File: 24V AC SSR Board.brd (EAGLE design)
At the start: 96.5 x 63.5 mm, 45 parts, among them X1 1751293

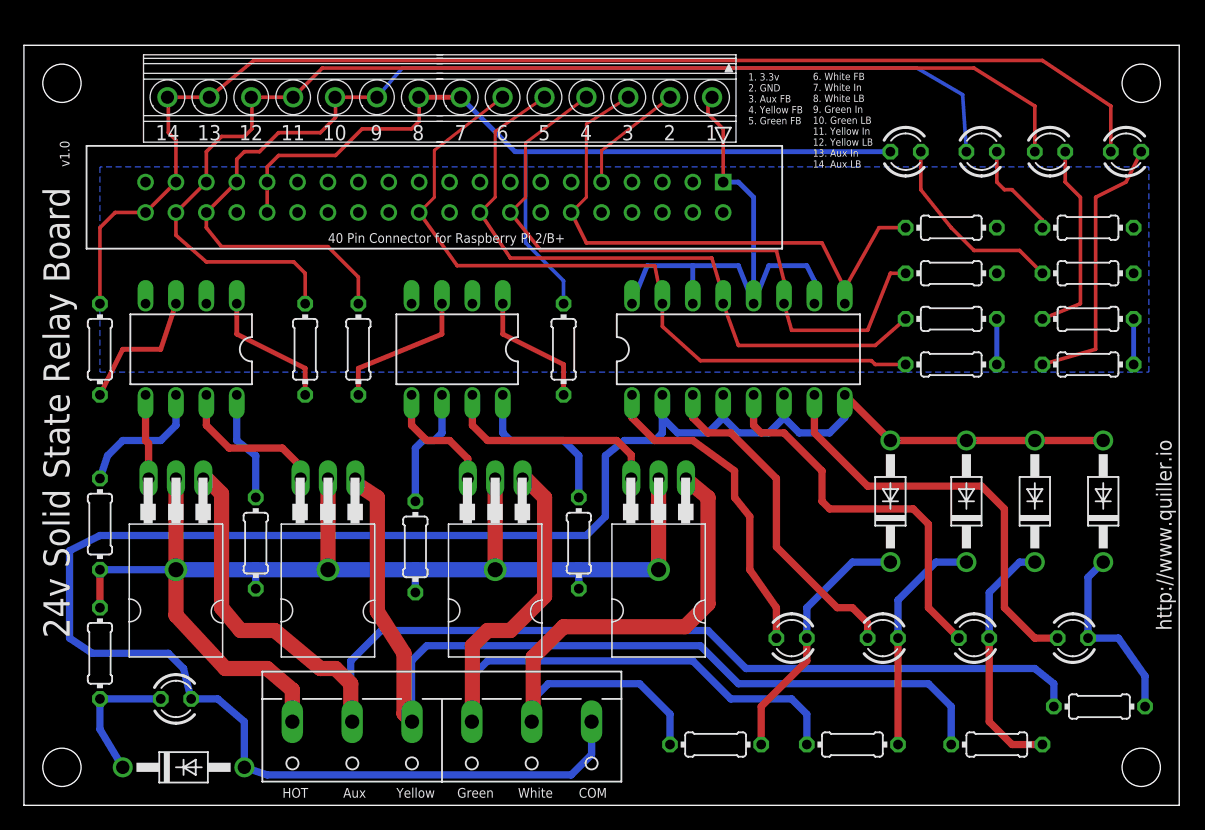
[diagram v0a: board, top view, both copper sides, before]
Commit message: Added Photon Board schematics and board
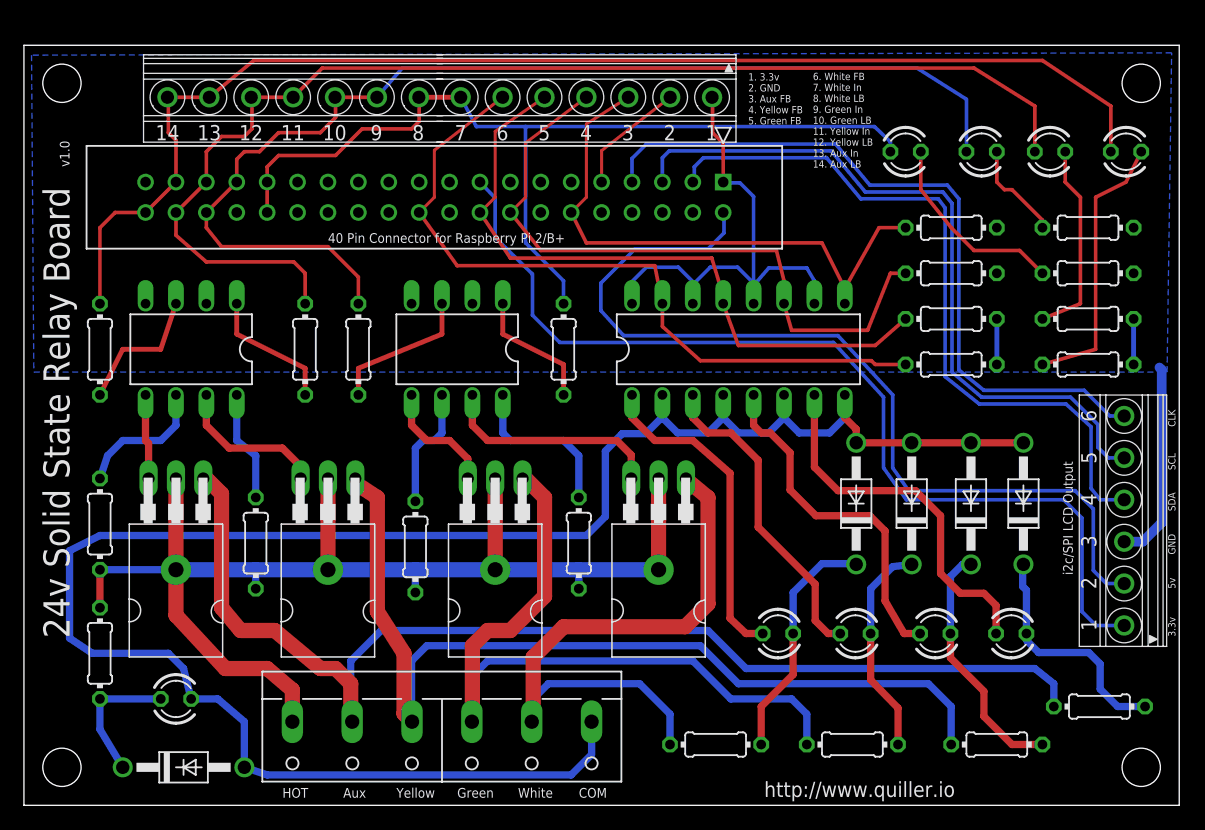
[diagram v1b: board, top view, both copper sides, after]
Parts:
- added T3-: (no value), myhvac:6-POS-SCREW-TERM-PT-3.5MM
- R18, R19, R20, R21: value 4.7K -> 100K
- TERM: value (none) -> OUT BLOCK
- moved D5 6.67 mm to (83.5, 25.2)
- moved D4 5.34 mm to (79.1, 25.2)
- moved LED_OUT_A 5.16 mm to (82.5, 14.4)
- moved D3 4.58 mm to (74.2, 25.2)
- moved LED_OUT_Y 3.26 mm to (76.1, 14.4)
- moved D2 2.86 mm to (69.5, 25.2)
- moved LED_OUT_G 2.32 mm to (69.5, 14.4)
- moved LED_OUT_W 1.20 mm to (63.0, 14.4)
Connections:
- net 3.3V_SOURCE renamed 3.3V_SRC1
- new net 3.3V-SRC2: IN.17, T3-.1
- new net 5V-SRC1: IN.2, T3-.2
- new net GCLK: IN.7, T3-.6
- new net SCL: IN.5, T3-.5
- new net SDA: IN.3, T3-.4
- net GND: now also T3-.3
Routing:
- net 3.3V-SRC2: track 0.00 -> 81.5 mm
- net 5V-SRC1: track 0.00 -> 76.2 mm
- net GCLK: track 0.00 -> 61.5 mm
- net SCL: track 0.00 -> 61.0 mm
- net SDA: track 0.00 -> 60.8 mm
- net GND: track 17.5 -> 34.3 mm
- net V-: track 170.5 -> 163.4 mm
- net N$14: track 35.4 -> 31.2 mm
- net N$30: track 15.8 -> 19.9 mm
- net N$13: track 32.6 -> 29.3 mm
- net WHITE_IN: track 75.4 -> 78.4 mm
- net N$11: track 28.2 -> 26.8 mm
- net N$21: track 21.6 -> 20.5 mm
- net N$22: track 19.1 -> 18.1 mm
- net 3.3V_SRC1: track 47.9 -> 47.3 mm
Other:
- board text added: "3.3v"
- board text added: "5v"
- board text added: "CLK"
- board text added: "GND"
- board text added: "SCL"
- board text added: "SDA"
- board text added: "i2c/SPI LCD Output"

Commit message: Added Temp Sensor gerber files.  General cleanup or bck files
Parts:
- moved T3- 1.52 mm to (90.3, 25.5)
- moved D2 1.11 mm to (68.6, 24.6)
- moved D4 1.11 mm to (78.2, 24.6)
- moved D3 0.95 mm to (73.4, 24.6)
- moved D5 0.95 mm to (82.7, 24.6)
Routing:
- net N$21: track 20.5 -> 18.9 mm
- net SDA: track 60.8 -> 59.2 mm
- net GCLK: track 61.5 -> 60.0 mm
- net SCL: track 61.0 -> 59.6 mm
- net 5V-SRC1: track 76.2 -> 74.8 mm
- net N$23: track 20.8 -> 19.7 mm
- net N$22: track 18.1 -> 17.1 mm
- net 3.3V-SRC2: track 81.5 -> 80.5 mm
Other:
- board text added: "40 Pin Connector for Raspberry Pi 3/2/B+"
- board text removed: "40 Pin Connector for Raspberry Pi 2/B+"
- board text removed: "CLK"
